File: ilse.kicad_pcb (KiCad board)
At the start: 2 copper layers, 81 x 109.5 mm, 87 parts, among them J1 OUT, J2 EURO RACK POWER, J3 CV Inputs, J4 1V/Oct, J5 Gate, J6 Cutoff, J7 Filter In, Q1 BC559, Q2 BC559, Q3 BC559, Q4 BC548, Q5 BC548, Q6 BC548, SW1 LFO to Filter / Freq CV, SW2 Resonance, U1 TL074, U2 TL074

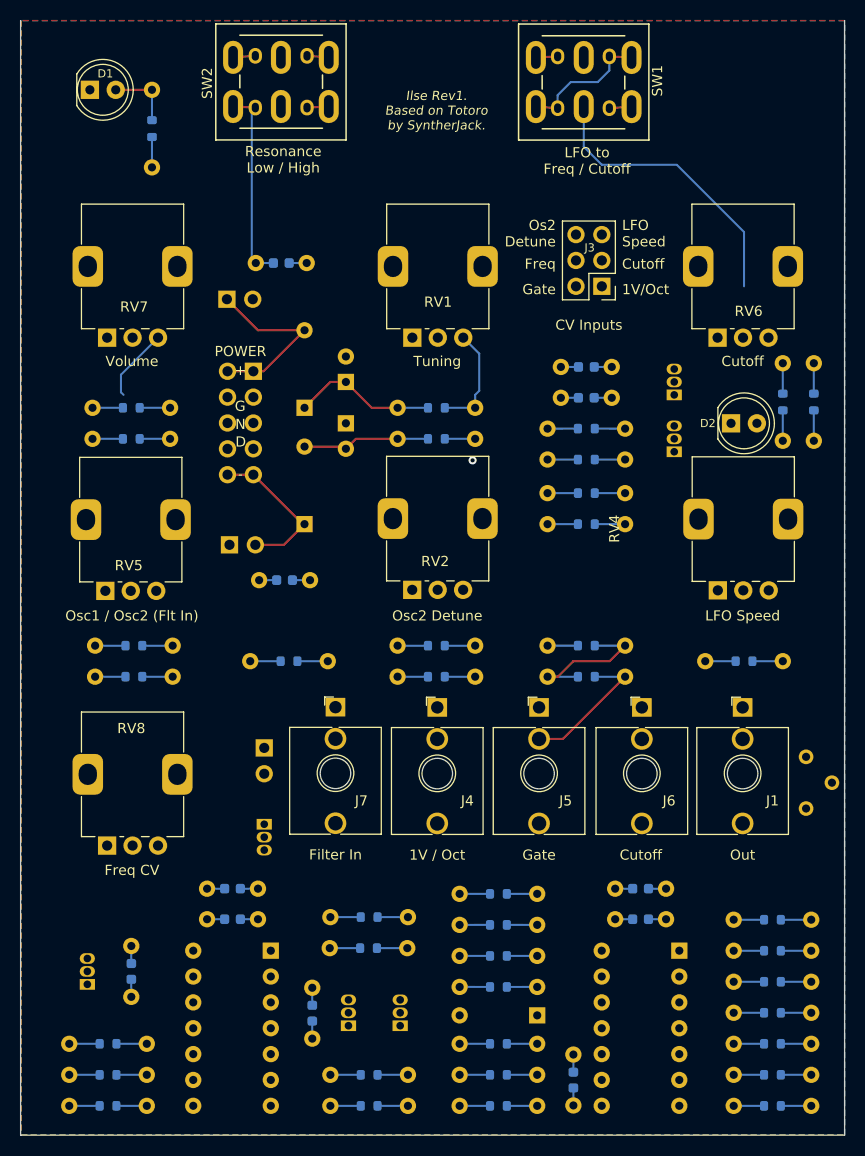
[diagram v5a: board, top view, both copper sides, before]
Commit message: finished routing and squashed DRC errors down to 0
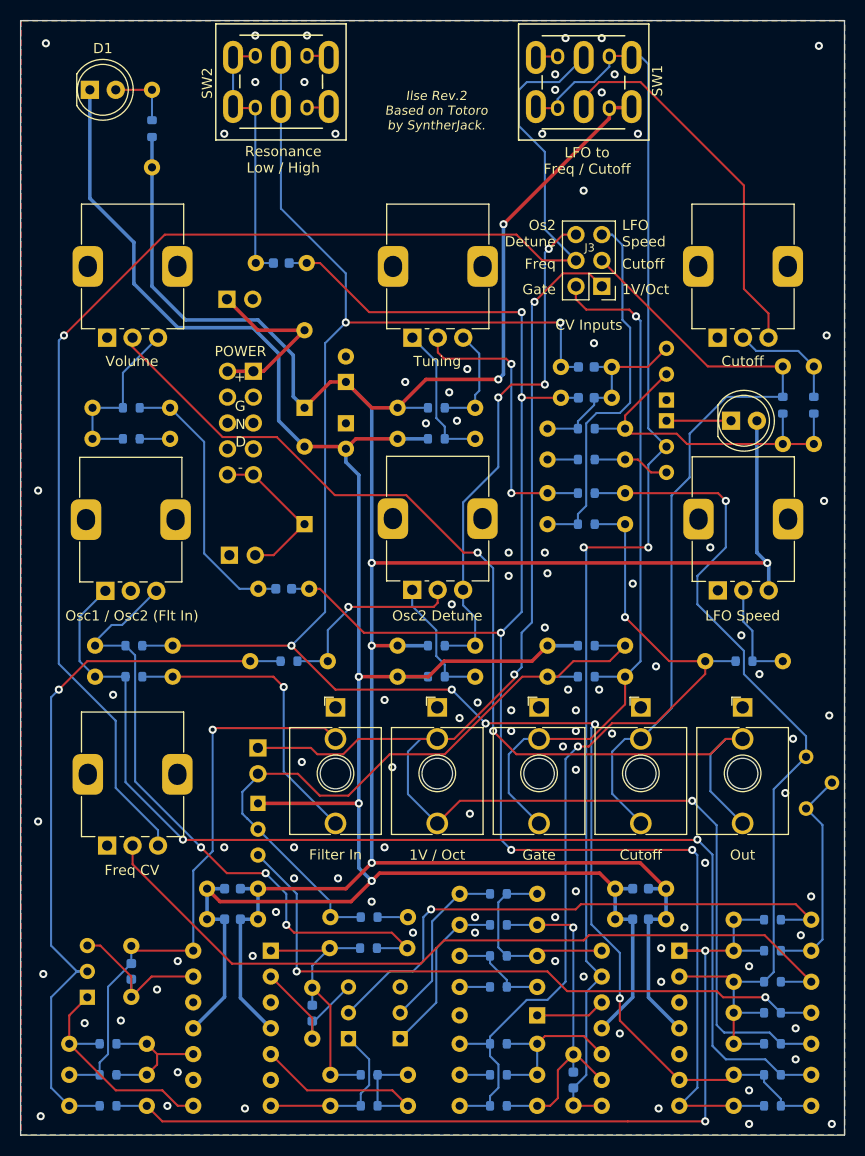
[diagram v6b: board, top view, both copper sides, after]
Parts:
- Q1, Q2, Q3, Q4, Q5, Q6: footprint Package_TO_SOT_THT:TO-92_Inline -> Package_TO_SOT_THT:TO-92_Inline_Wide
- moved Q6 3.14 mm to (154.7, 75.7), turned to -90 degrees
- moved Q1 2.14 mm to (114.6, 113.3)
- moved Q2 1.27 mm to (123.5, 136.4)
- moved Q3 1.27 mm to (97.9, 132.3)
- moved Q4 1.27 mm to (128.6, 136.4)
- moved LOGO1 1.15 mm to (131.4, 47.2)
- moved BT2 1.02 mm to (111.8, 88.9)
- moved Q5 0.92 mm to (154.7, 73.7)
- moved C11 0.85 mm to (119.6, 92.2)
- moved JP1 0.62 mm to (114.6, 107.8)
- moved R30 0.32 mm to (169.2, 70.4)
- moved R33 0.32 mm to (166.2, 70.4)
- moved D2 0.25 mm to (161.1, 75.7)
- moved J6 0.10 mm to (152.2, 103.9)
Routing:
- net VCC: track 11.2 -> 266.0 mm, vias 0 -> 6
- net VSS: track 9.64 -> 203.3 mm, vias 0 -> 3
- net Net-(C8-Pad1): track 0.00 -> 180.8 mm, vias 0 -> 7
- net Net-(C10-Pad2): track 0.00 -> 150.9 mm, vias 0 -> 5
- net 1V/Oct: track 0.00 -> 142.4 mm, vias 0 -> 3
- net Freq CV: track 0.00 -> 136.6 mm, vias 0 -> 1
- net Net-(C7-Pad2): track 8.74 -> 123.3 mm, vias 0 -> 2
- net Net-(R18-Pad1): track 0.00 -> 107.4 mm, vias 0 -> 2
- net Net-(J1-PadT): track 0.00 -> 99.3 mm, vias 0 -> 2
- net Net-(R15-Pad1): track 0.00 -> 83.2 mm, vias 0 -> 2
- net Filter Cutoff: track 0.00 -> 76.4 mm
- net Net-(R19-Pad1): track 0.00 -> 76.3 mm, vias 0 -> 2
- net Net-(R36-Pad1): track 0.00 -> 76.0 mm, vias 0 -> 1
- net Net-(R36-Pad2): track 0.00 -> 75.6 mm
- net Net-(Q3-Pad2): track 0.00 -> 66.1 mm, vias 0 -> 1
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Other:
- board size 81 x 109.5 mm -> 80.9 x 109.5 mm
- board text added: "Ilse Rev.2 Based on Totoro by SyntherJack."
- board text removed: "Ilse Rev1. Based on Totoro by SyntherJack."
